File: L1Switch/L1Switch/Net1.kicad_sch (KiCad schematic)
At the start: 66 parts, among them J8 Conn_01x07_Male, U9 VSC8658

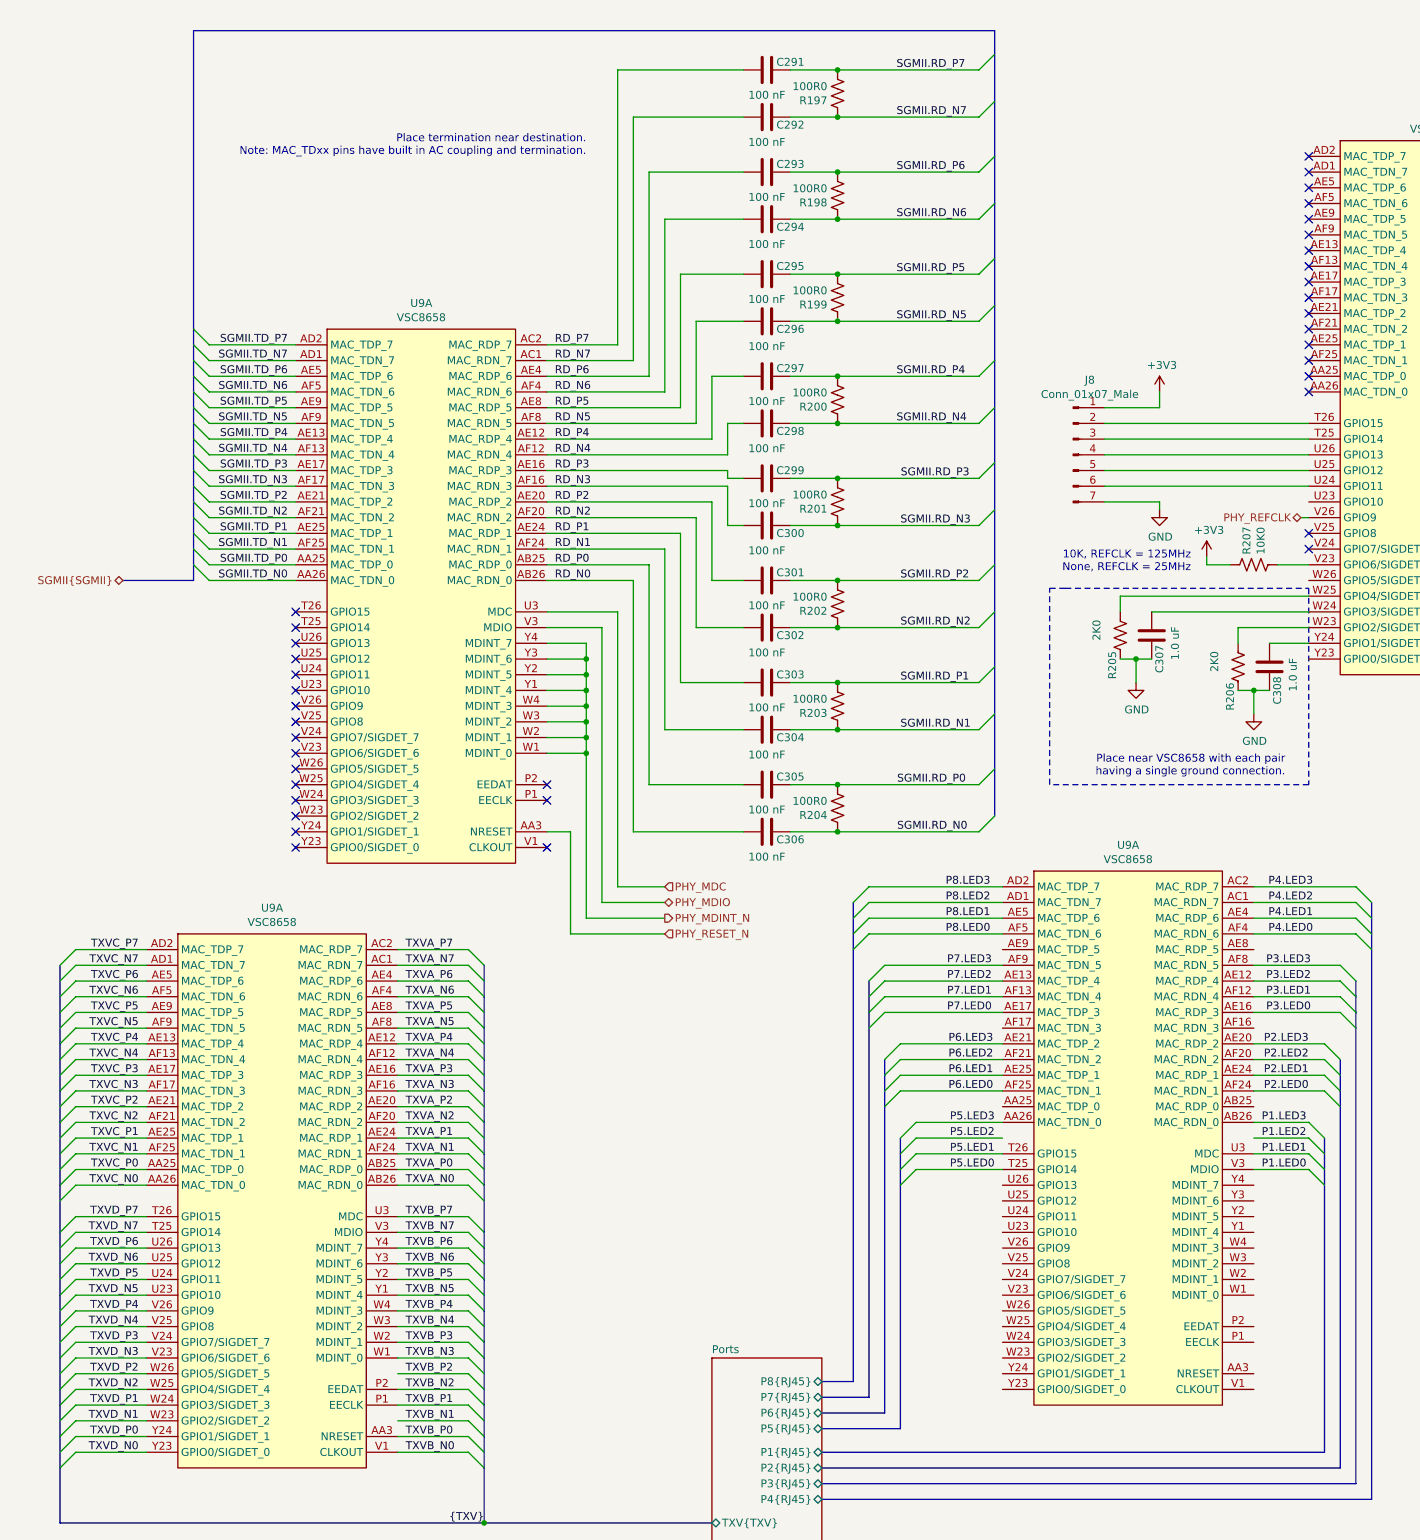
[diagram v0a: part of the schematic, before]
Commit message: Swap fan connector orientation. Add PU/PD for JTAG pins.
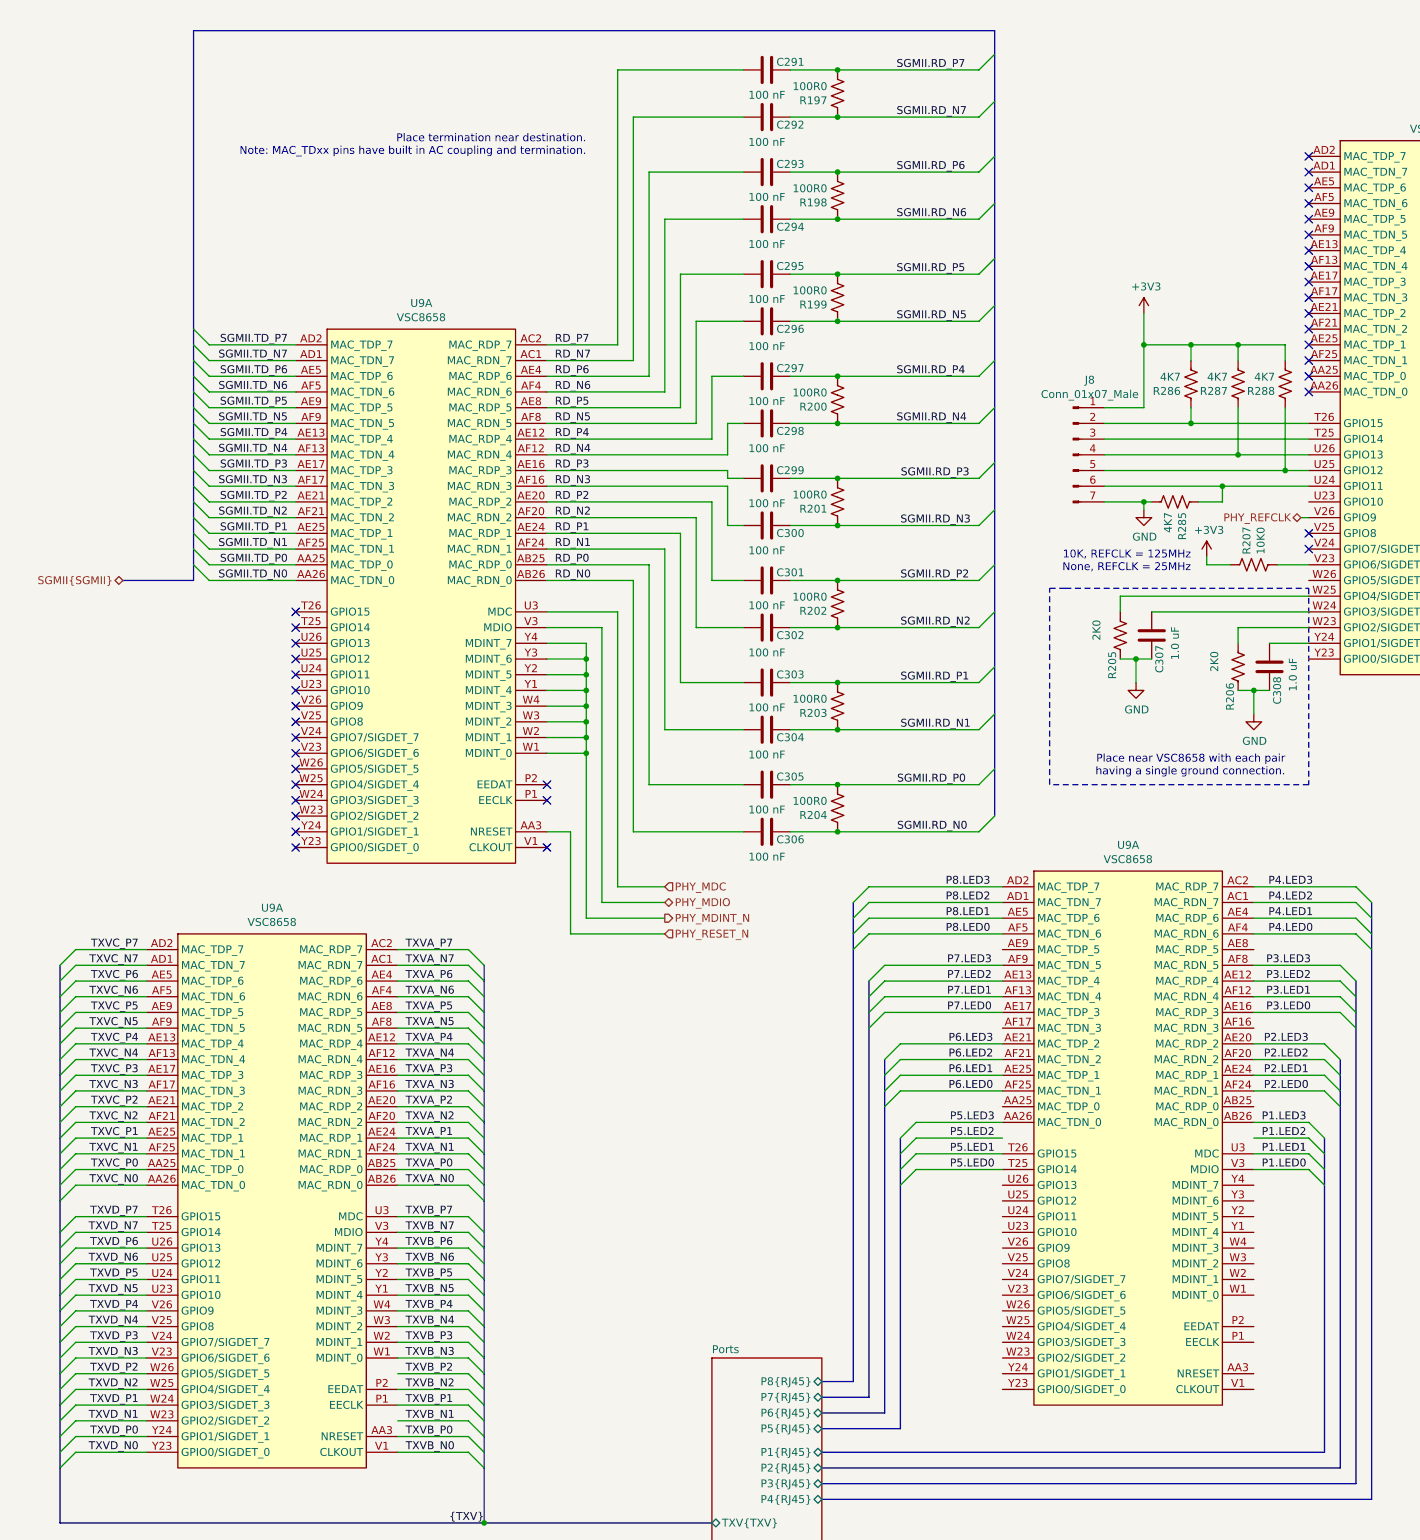
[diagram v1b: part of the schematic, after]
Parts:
- added R285, R286, R287, R288: 4K7, Resistor_SMD:R_0402_1005Metric, symbol Device:R_US
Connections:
- net +3V3: now also R286.2, R287.2, R288.2
- net GND: now also R285.2
- net at J8.2 (Pin_2), U9.T26 (GPIO15): now also R286.1
- net at J8.6 (Pin_6), U9.U24 (GPIO11): now also R285.1
- net at J8.5 (Pin_5), U9.U25 (GPIO12): now also R288.1
- net at J8.4 (Pin_4), U9.U26 (GPIO13): now also R287.1

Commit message: Update RJ45 pinout on schematic and partial layout update.
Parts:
- renumbered C315 to C100, C316 to C101, C320 to C102, C321 to C103, C322 to C104, C323 to C105, C324 to C106, C325 to C107, C326 to C108, C327 to C109, C291 to C11, C328 to C110, C329 to C111, C330 to C112, C331 to C113, C332 to C114, C333 to C115, C334 to C116, C335 to C117, C317 to C118, C318 to C119, C292 to C12, C319 to C120, C293 to C13, C294 to C14, C295 to C15, C296 to C16, C297 to C17, C298 to C18, C299 to C19, C300 to C20, C301 to C21, C302 to C22, C303 to C23, C304 to C24, C305 to C25, C306 to C26, C307 to C27, C308 to C28, C309 to C94, C310 to C95, C311 to C96, C312 to C97, C313 to C98, C314 to C99, FB4 to FB1, J8 to J2, R198 to R10, R199 to R11, R200 to R12, R201 to R13, R202 to R14, R203 to R15, R204 to R16, R205 to R18, R206 to R19, R207 to R20, R285 to R273, R286 to R274, R287 to R275, R288 to R276, R197 to R9, U9 to U2

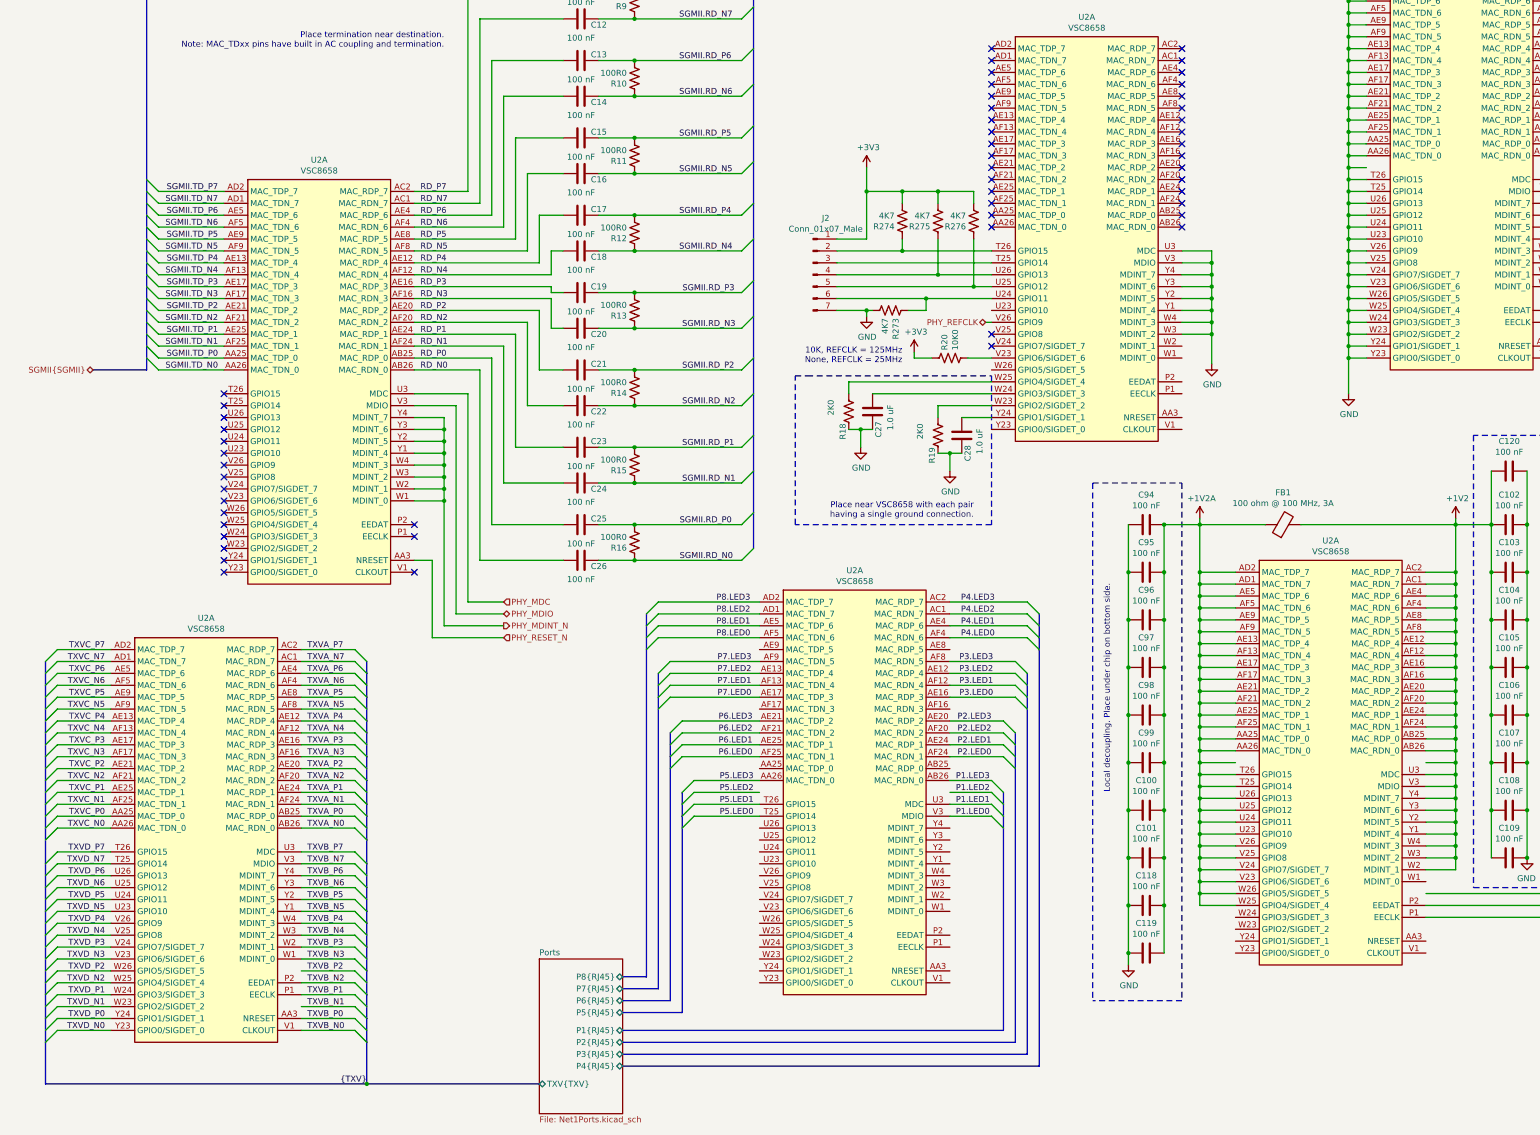
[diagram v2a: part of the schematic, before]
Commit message: Add PWR_FLAG to clean up ERC errors about undriven nets. Change R269 from 100K0 to 10K0.
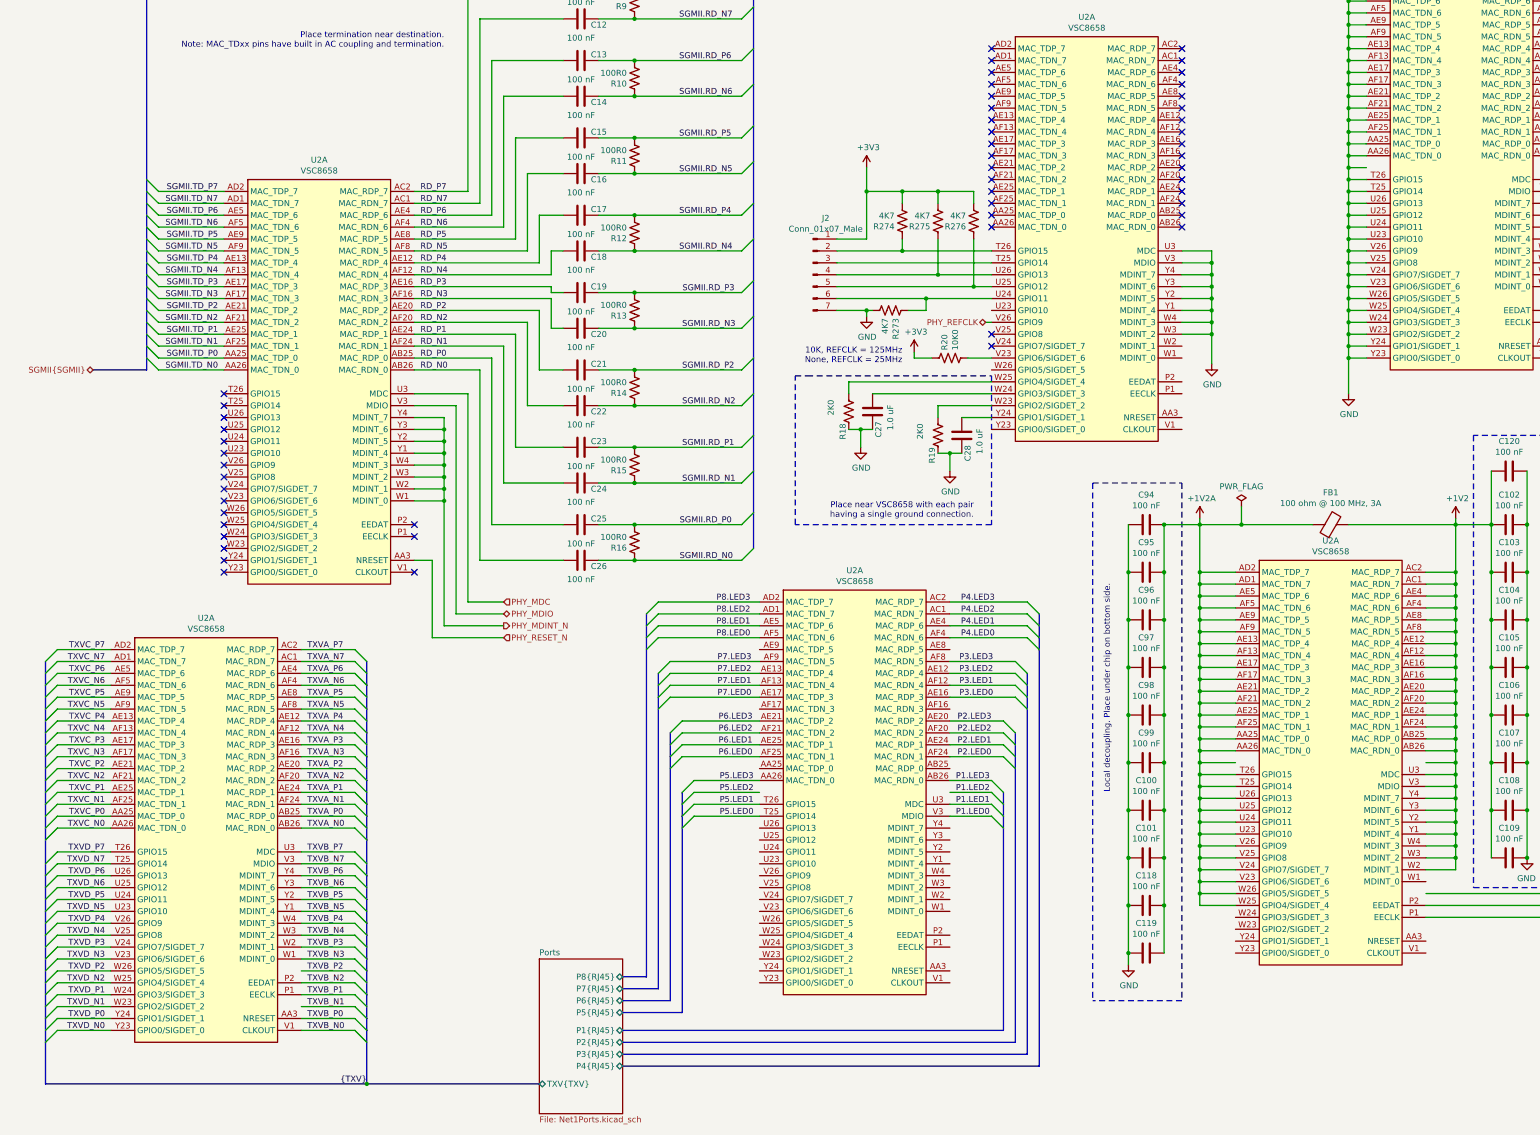
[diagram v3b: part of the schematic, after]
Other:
- moved on the sheet: FB1

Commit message: Update voltage monitoring.
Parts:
- renumbered C11 to C291, C12 to C292, C13 to C293, C14 to C294, C15 to C295, C16 to C296, C17 to C297, C18 to C298, C19 to C299, C20 to C300, C21 to C301, C22 to C302, C23 to C303, C24 to C304, C25 to C305, C26 to C306, C27 to C307, C28 to C308, C94 to C309, C95 to C310, C96 to C311, C97 to C312, C98 to C313, C99 to C314, C100 to C315, C101 to C316, C118 to C317, C119 to C318, C120 to C319, C102 to C320, C103 to C321, C104 to C322, C105 to C323, C106 to C324, C107 to C325, C108 to C326, C109 to C327, C110 to C328, C111 to C329, C112 to C330, C113 to C331, C114 to C332, C115 to C333, C116 to C334, C117 to C335, FB1 to FB4, J2 to J8, R9 to R197, R10 to R198, R11 to R199, R12 to R200, R13 to R201, R14 to R202, R15 to R203, R16 to R204, R18 to R205, R19 to R206, R20 to R207, R273 to R285, R274 to R286, R275 to R287, R276 to R288, U2 to U9
